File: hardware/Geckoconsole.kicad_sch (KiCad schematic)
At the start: 60 parts, among them J1 Conn_01x08_Male, J31 Conn_01x07_Female, J50 USB-C, J70 I²C, J71 I²C, J81 Conn_01x07, Q51 S8050, Q52 S8050, SW2 Reset, SW41 Rotary_Encoder_Switch, SW42 Button2, U1 ESP32-WROOM-32, U101 AMS1117-3.3, U2 CP2102, U70 VCNL4040M3OE

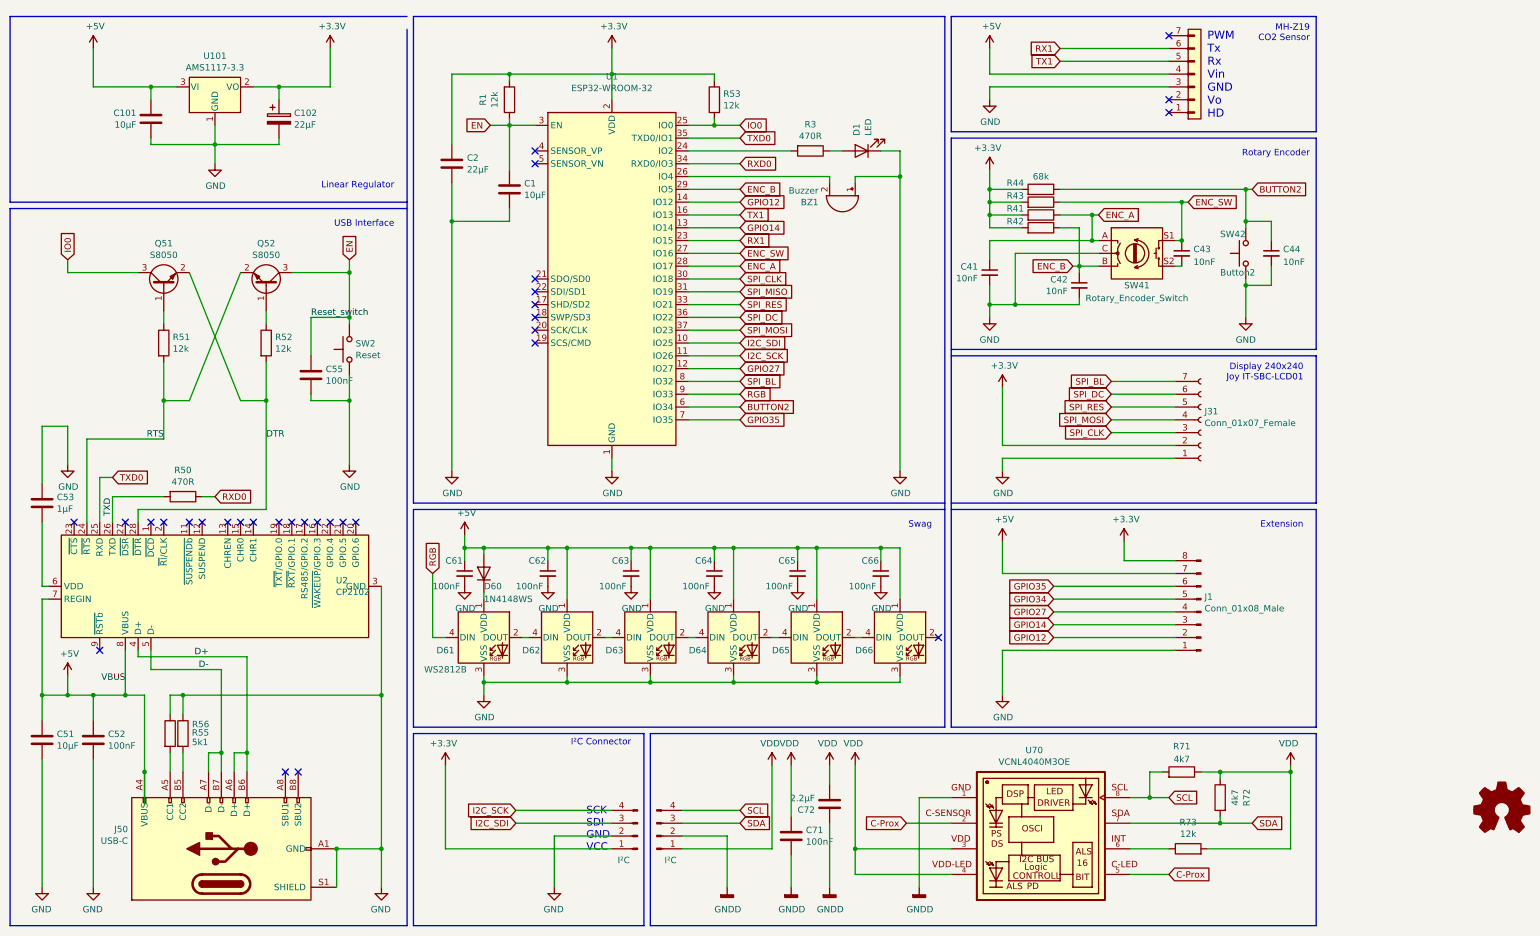
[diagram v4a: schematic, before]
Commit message: Hardware Console: Start with HW Revision 2
* include 2nd navigation button
* move USB-C interface onto separate daughter board
* hide VCNL4040 parts from PCB
* turn ESP32 180°
* move LCD pin header to top of board
* switch a few GPIOs
* place parts on PCB
* TBD: Routing
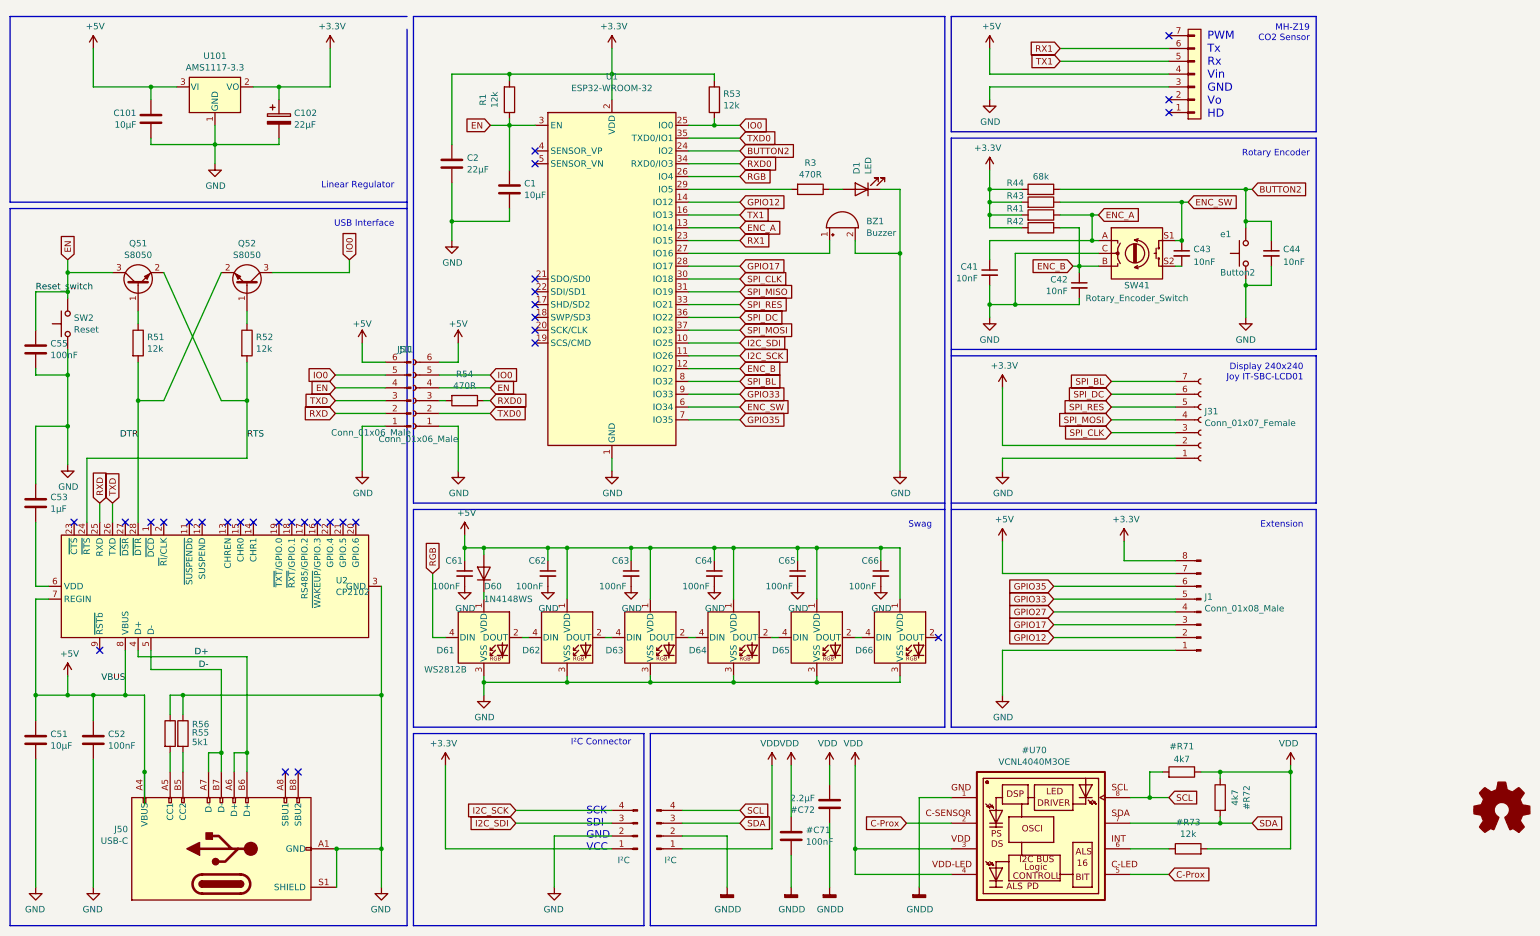
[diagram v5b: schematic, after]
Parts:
- removed R50: 470R, Resistor_SMD:R_0805_2012Metric_Pad1.20x1.40mm_HandSolder, symbol Device:R
- added J11: Conn_01x06_Male, Connector_PinSocket_2.00mm:PinSocket_1x06_P2.00mm_Horizontal, symbol Connector:Conn_01x06_Female
- added J51: Conn_01x06_Male, Connector_PinHeader_2.00mm:PinHeader_1x06_P2.00mm_Horizontal, symbol Connector:Conn_01x06_Male
- added R54: 470R, Resistor_SMD:R_0805_2012Metric_Pad1.20x1.40mm_HandSolder, symbol Device:R
- e1: renamed from SW42; footprint Button_Switch_SMD:SW_SPST_B3U-1000P-B -> Button_Switch_THT:SW_PUSH_6mm_H5mm
- renumbered C71 to #C71, C72 to #C72, J71 to #J71, R71 to #R71, R72 to #R72, R73 to #R73, U70 to #U70
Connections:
- net +5V: now also J11.6 (Pin_6), J51.6 (Pin_6)
- net BUTTON2: now also U1.24 (IO2); no longer U1.6 (IO34)
- net DTR: now also Q52.2 (E), R51.2; no longer Q51.2 (E), R52.2
- net EN: now also Q51.3 (C), J11.4 (Pin_4), J51.4 (Pin_4); no longer Q52.3 (C)
- net ENC_A: now also U1.13 (IO14); no longer U1.28 (IO17)
- net ENC_B: now also U1.12 (IO27); no longer U1.29 (IO5)
- net ENC_SW: now also U1.6 (IO34); no longer U1.27 (IO16)
- net GND: now also BZ1.2 (+), J11.1 (Pin_1), J51.1 (Pin_1); no longer BZ1.1 (-)
- net GPIO27: no longer U1.12 (IO27)
- net IO0: now also Q52.3 (C), J11.5 (Pin_5), J51.5 (Pin_5); no longer Q51.3 (C)
- net RGB: now also U1.26 (IO4); no longer U1.9 (IO33)
- net RTS: now also Q51.2 (E), R52.2; no longer Q52.2 (E), R51.2
- net RXD0: now also R54.1
- net TXD: now also J51.3 (Pin_3)
- net TXD0: now also J11.2 (Pin_2); no longer U2.25 (RXD)
- net at R3.2: now also U1.29 (IO5); no longer U1.24 (IO2)
- net GPIO14 renamed GPIO17
- net GPIO17: now also U1.28 (IO17); no longer U1.13 (IO14)
- net GPIO34 renamed GPIO33
- net GPIO33: now also U1.9 (IO33)
- new net: BZ1.1 (-), U1.27 (IO16)
- new net: J11.3 (Pin_3), R54.2
- new net RXD: J51.2 (Pin_2), U2.25 (RXD)
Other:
- moved on the sheet: BZ1, C51, C53, C55, D1, Q51, Q52, R3, R51, R52, SW2

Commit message: Hardware Console: Route USB daughter board & some more GPIO shuffling
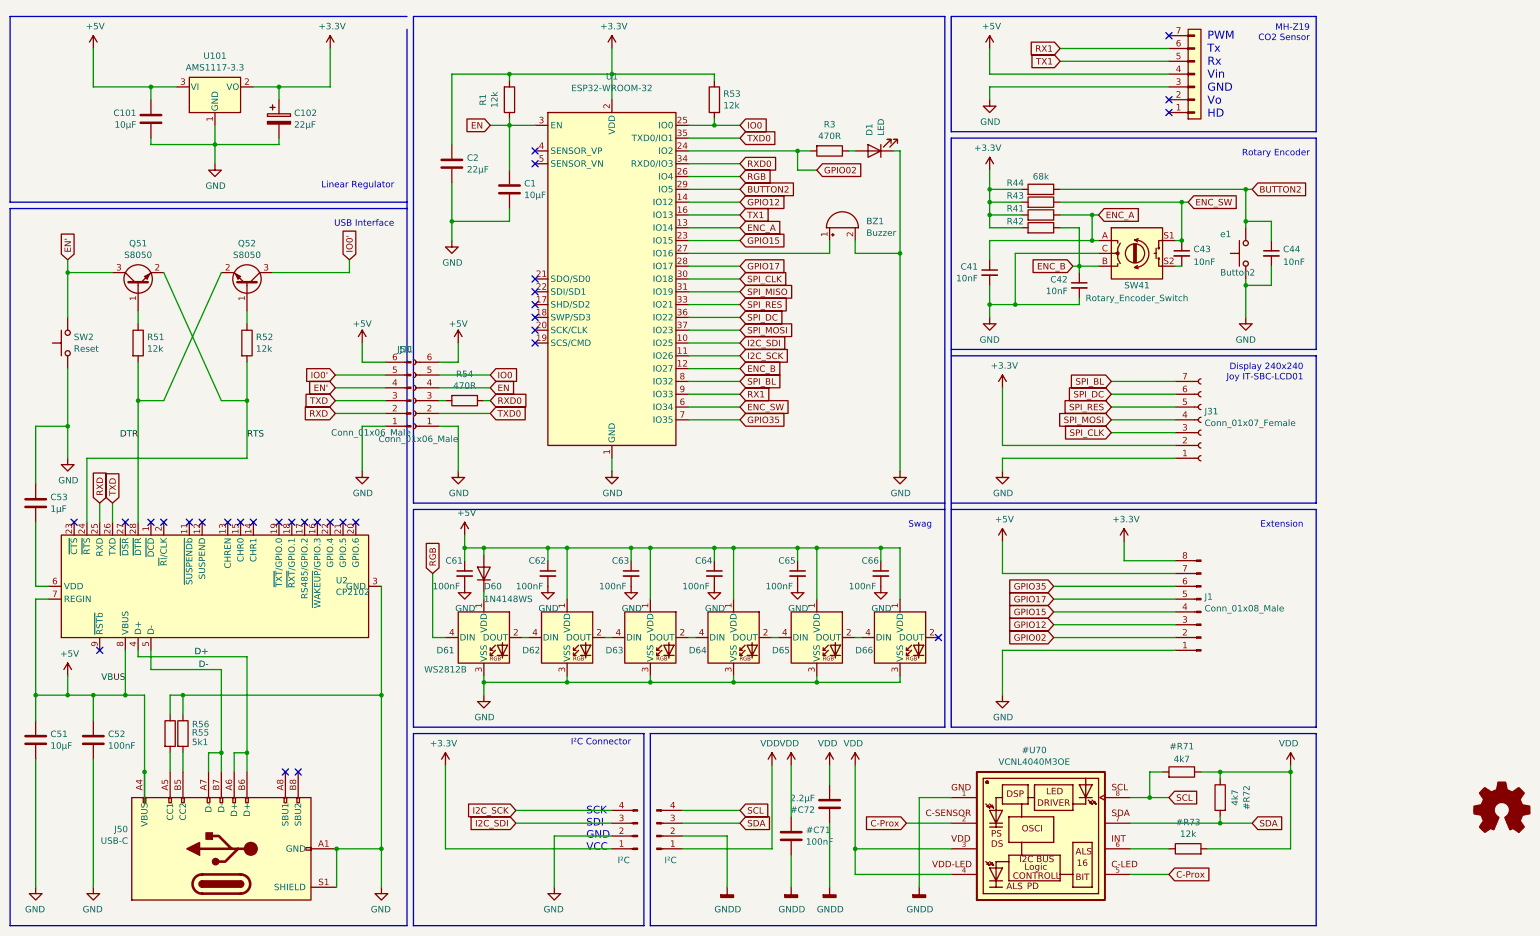
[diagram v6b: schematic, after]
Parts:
- removed C55: 100nF, Capacitor_SMD:C_0603_1608Metric_Pad1.08x0.95mm_HandSolder, symbol Device:C
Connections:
- net BUTTON2: now also U1.29 (IO5); no longer U1.24 (IO2)
- net EN: no longer J51.4 (Pin_4), Q51.3 (C), SW2.2
- net GPIO12: now also J1.3 (Pin_3); no longer J1.2 (Pin_2)
- net GPIO17: now also J1.5 (Pin_5); no longer J1.3 (Pin_3)
- net IO0: no longer J51.5 (Pin_5), Q52.3 (C)
- net RX1: now also U1.9 (IO33); no longer U1.23 (IO15)
- net GPIO02: now reaches R3.2
- net GPIO02: now also J1.2 (Pin_2), U1.24 (IO2); no longer U1.29 (IO5)
- net GPIO27 renamed GPIO15
- net GPIO15: now also U1.23 (IO15)
- removed net GPIO33: J1.5 (Pin_5), U1.9 (IO33)
- new net EN': J51.4 (Pin_4), Q51.3 (C), SW2.2
- new net IO0': J51.5 (Pin_5), Q52.3 (C)
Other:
- moved on the sheet: D1, R3, SW2

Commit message: Hardware Console: Route PCB, Pannelize
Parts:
- J1: value Conn_01x08_Male -> Conn_01x06_Male; footprint Connector_PinHeader_2.54mm:PinHeader_2x04_P2.54mm_Vertical -> Connector_PinHeader_2.54mm:PinHeader_2x03_P2.54mm_Vertical; symbol Connector:Conn_01x08_Male -> Connector:Conn_01x06_Male
- renumbered SW2 to SW1, e1 to SW2
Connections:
- net +3V3: now also J1.6 (Pin_6); no longer J1.8 (Pin_8)
- net +5V: no longer C61.1, J1.7 (Pin_7)
- net ENC_A: now also U1.12 (IO27); no longer U1.13 (IO14)
- net ENC_B: now also U1.13 (IO14); no longer U1.12 (IO27)
- net GPIO12: now also J1.2 (Pin_2); no longer J1.3 (Pin_3)
- net GPIO15: now also J1.3 (Pin_3); no longer J1.4 (Pin_4)
- net GPIO17: now also J1.4 (Pin_4); no longer J1.5 (Pin_5)
- net GPIO35: now also J1.5 (Pin_5); no longer J1.6 (Pin_6)
- net at D60.1 (K), D61.1 (VDD): now also C61.1
- net GPIO02: no longer names the net of R3.2, U1.24 (IO2)
- net GPIO02: no longer J1.2 (Pin_2)
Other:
- moved on the sheet: D60

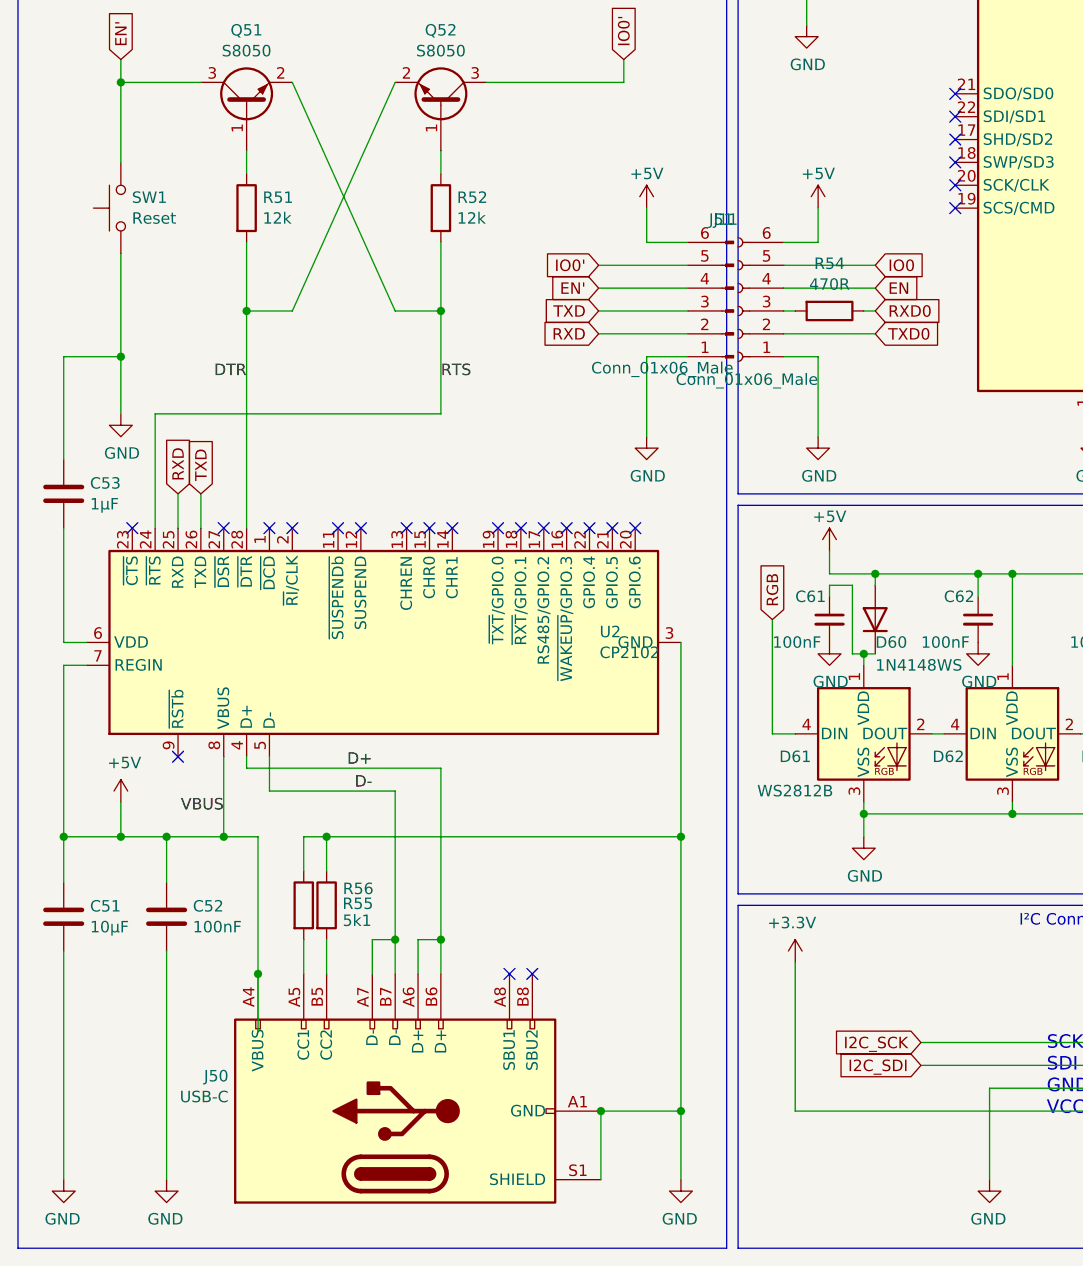
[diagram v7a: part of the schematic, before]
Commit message: Hardware Console: Improve Layout: DRC, Mouse Bites, placement, silkscreen
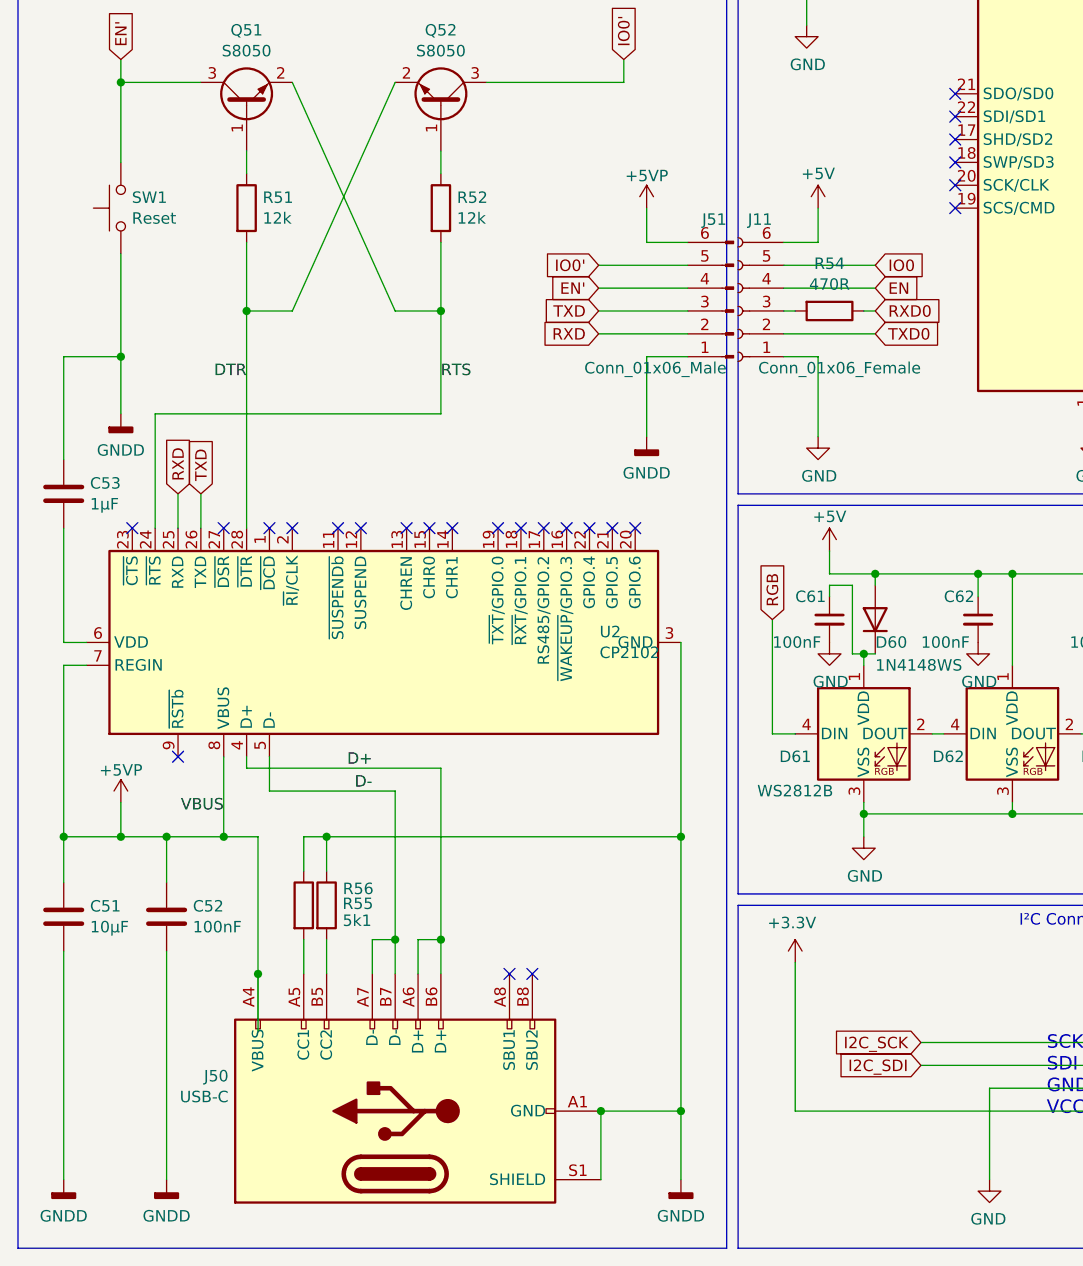
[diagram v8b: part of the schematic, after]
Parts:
- D61, D62, D63, D64, D65, D66: footprint LED_SMD:LED_WS2812B_PLCC4_5.0x5.0mm_P3.2mm -> Fraxinas:LED_WS2812B_PLCC4_5.0x5.0mm_P3.2mm_Marking
- J11: value Conn_01x06_Male -> Conn_01x06_Female
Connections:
- net +5V: no longer C51.1, C52.1, J50.A4 (VBUS), J50.A9 (VBUS), J50.B4 (VBUS), J50.B9 (VBUS), J51.6 (Pin_6), U2.7 (REGIN), U2.8 (VBUS)
- net GND: no longer C51.2, C52.2, C53.1, J50.A1 (GND), J50.A12 (GND), J50.B1 (GND), J50.B12 (GND), J50.S1 (SHIELD), J51.1 (Pin_1), R55.1, R56.1, SW1.1, U2.29 (GND), U2.3 (GND)
- net GNDD: now also C51.2, C52.2, C53.1, J50.A1 (GND), J50.A12 (GND), J50.B1 (GND), J50.B12 (GND), J50.S1 (SHIELD), J51.1 (Pin_1), R55.1, R56.1, SW1.1, U2.29 (GND), U2.3 (GND)
- new net +5VP: C51.1, C52.1, J50.A4 (VBUS), J50.A9 (VBUS), J50.B4 (VBUS), J50.B9 (VBUS), J51.6 (Pin_6), U2.7 (REGIN), U2.8 (VBUS)
